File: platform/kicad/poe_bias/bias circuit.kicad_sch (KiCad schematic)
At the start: 10 parts, among them J1 Screw_Terminal_01x06, J2 Screw_Terminal_01x06

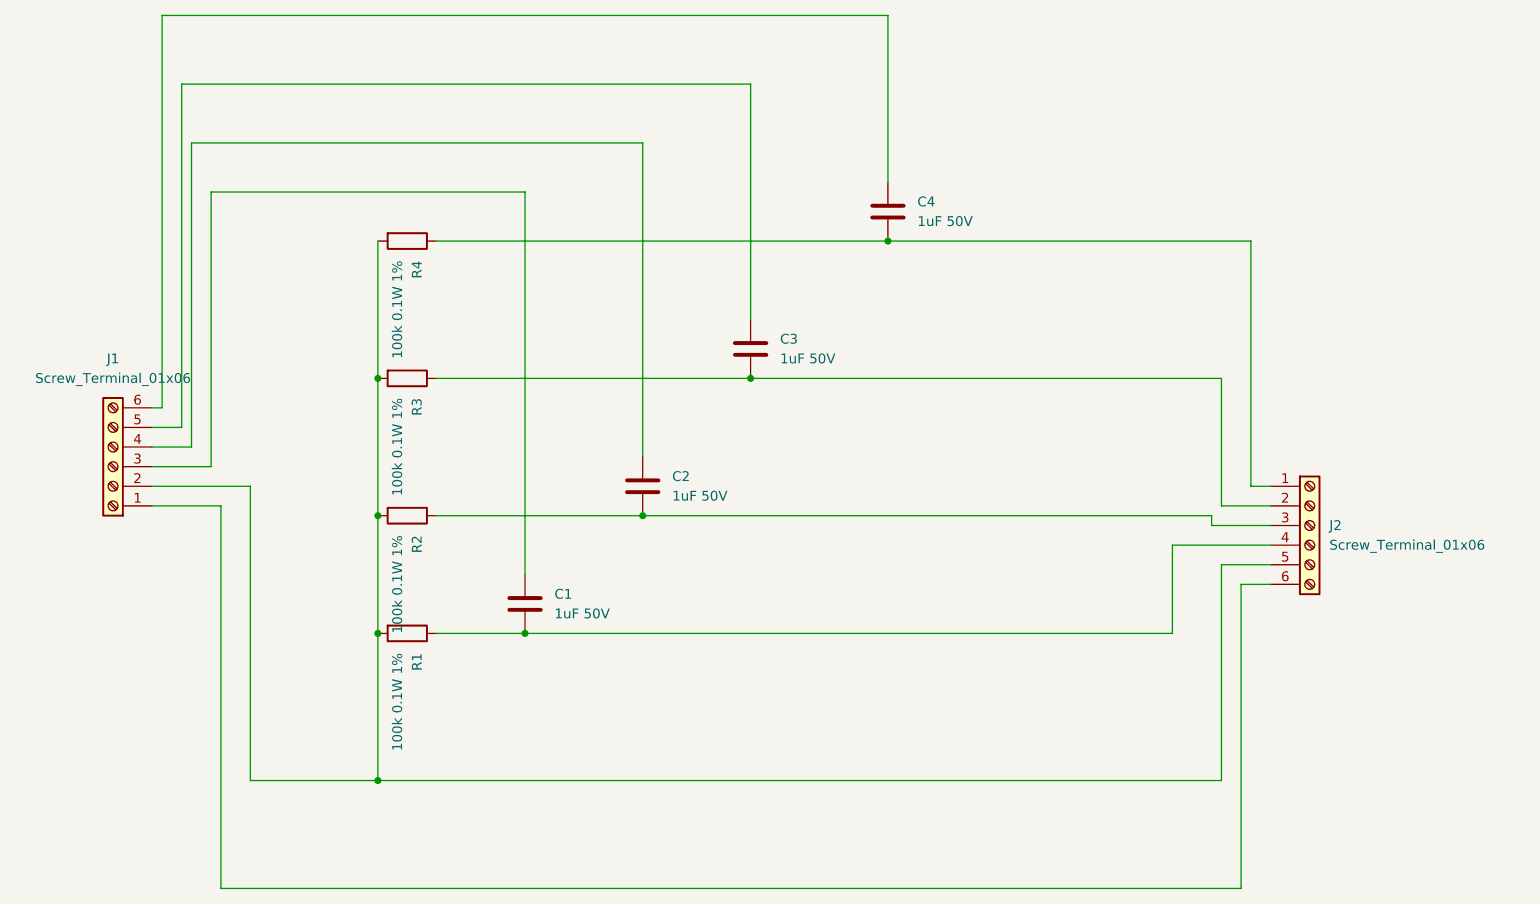
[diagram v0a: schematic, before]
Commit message: PoE Bias: Update PCB layout
This change shrinks the profile of the PCB, as well as adding mounting holes and labelling.
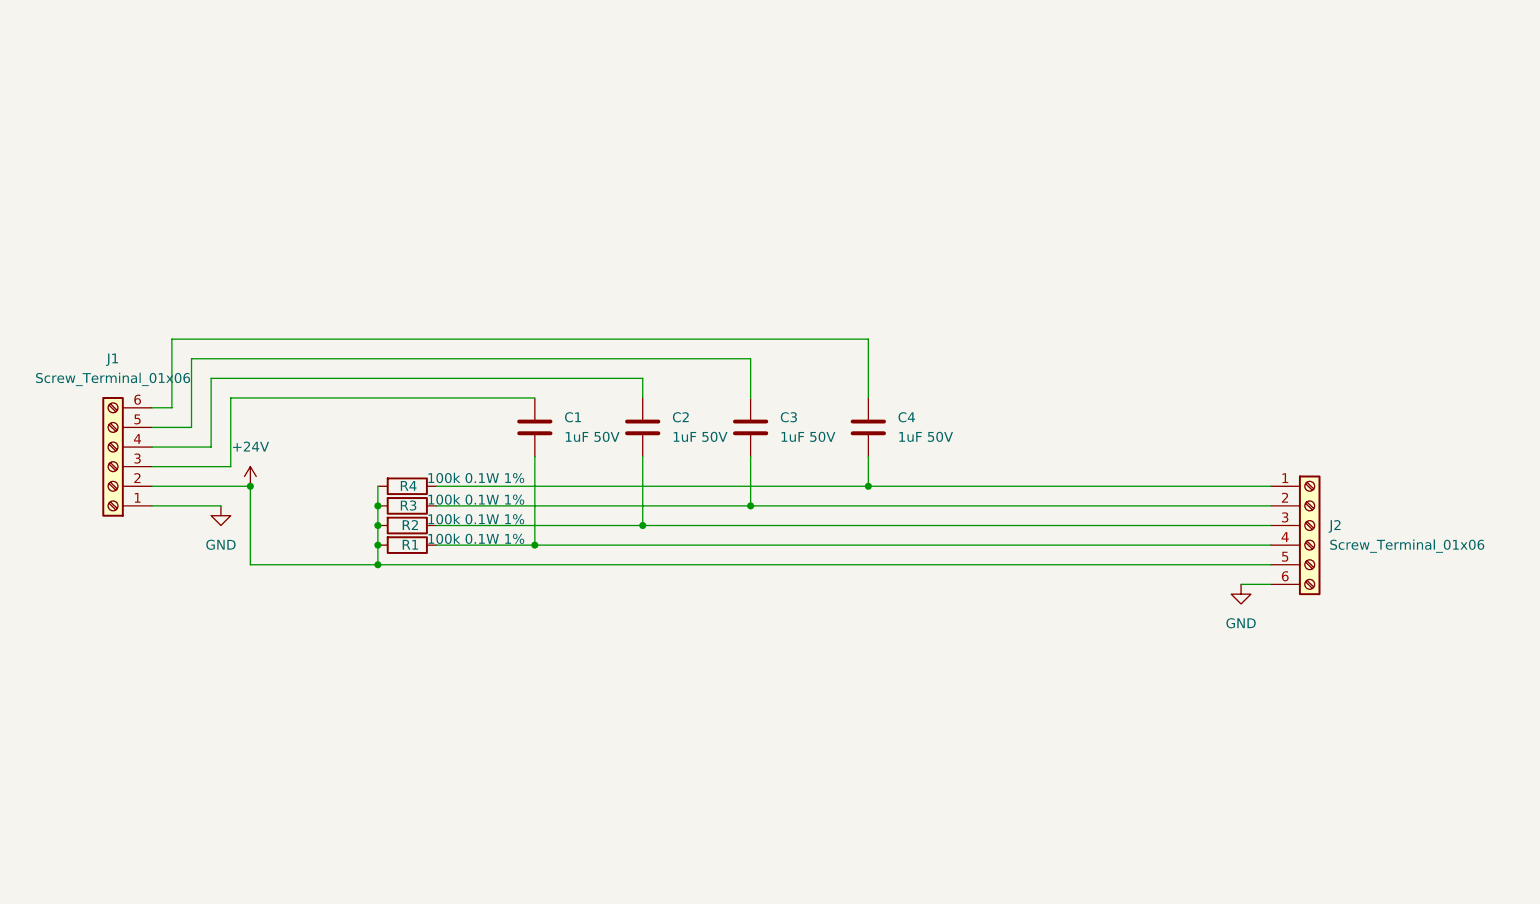
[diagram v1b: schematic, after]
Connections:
- net GND: now reaches J1.1 (Pin_1), J2.6 (Pin_6)
- net +24V: now reaches J1.2 (Pin_2), J2.5 (Pin_5), R1.2, R2.2, R3.2, R4.2
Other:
- moved on the sheet: C1, C2, C3, C4, R1, R2, R3, R4
